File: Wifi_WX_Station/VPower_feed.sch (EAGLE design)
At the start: 5 parts, among them J1 RJ45-8VERT, J2 RJ45-8VERT

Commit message: updated BOM with all prices- As Checked in to BATCH PCB
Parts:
- RAIN, SUN: device wifi_WX:PINHD-1X3 -> wifi_WX:PINHD-1X3MOLEX_KK
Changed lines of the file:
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@@
 <part name="SUPPLY11" library="supply2" deviceset="GND" device=""/>
 <part name="P+3" library="supply1" deviceset="+5V" device=""/>
-<part name="RAIN" library="wifi_WX" deviceset="PINHD-1X3" device=""/>
-<part name="SUN" library="wifi_WX" deviceset="PINHD-1X3" device=""/>
+<part name="RAIN" library="wifi_WX" deviceset="PINHD-1X3" device="MOLEX_KK"/>
+<part name="SUN" library="wifi_WX" deviceset="PINHD-1X3" device="MOLEX_KK"/>
 </parts>
 <sheets>

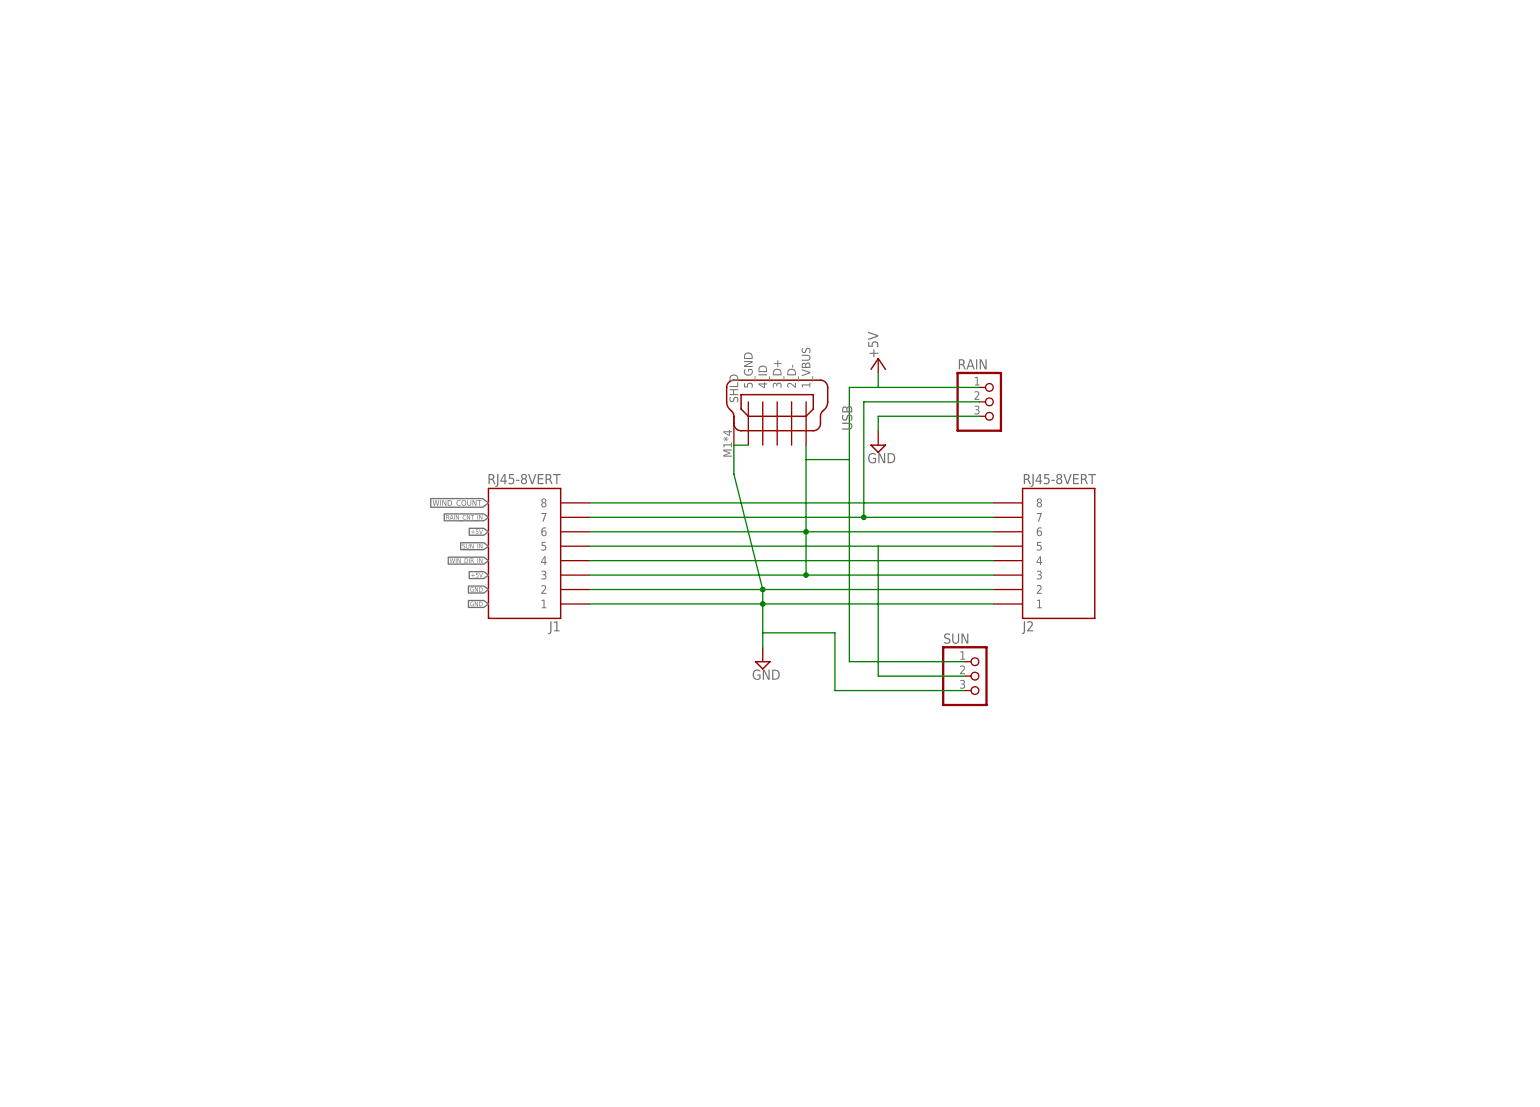
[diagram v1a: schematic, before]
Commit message: added SILabs Hygrometer board Added frames to the schematics
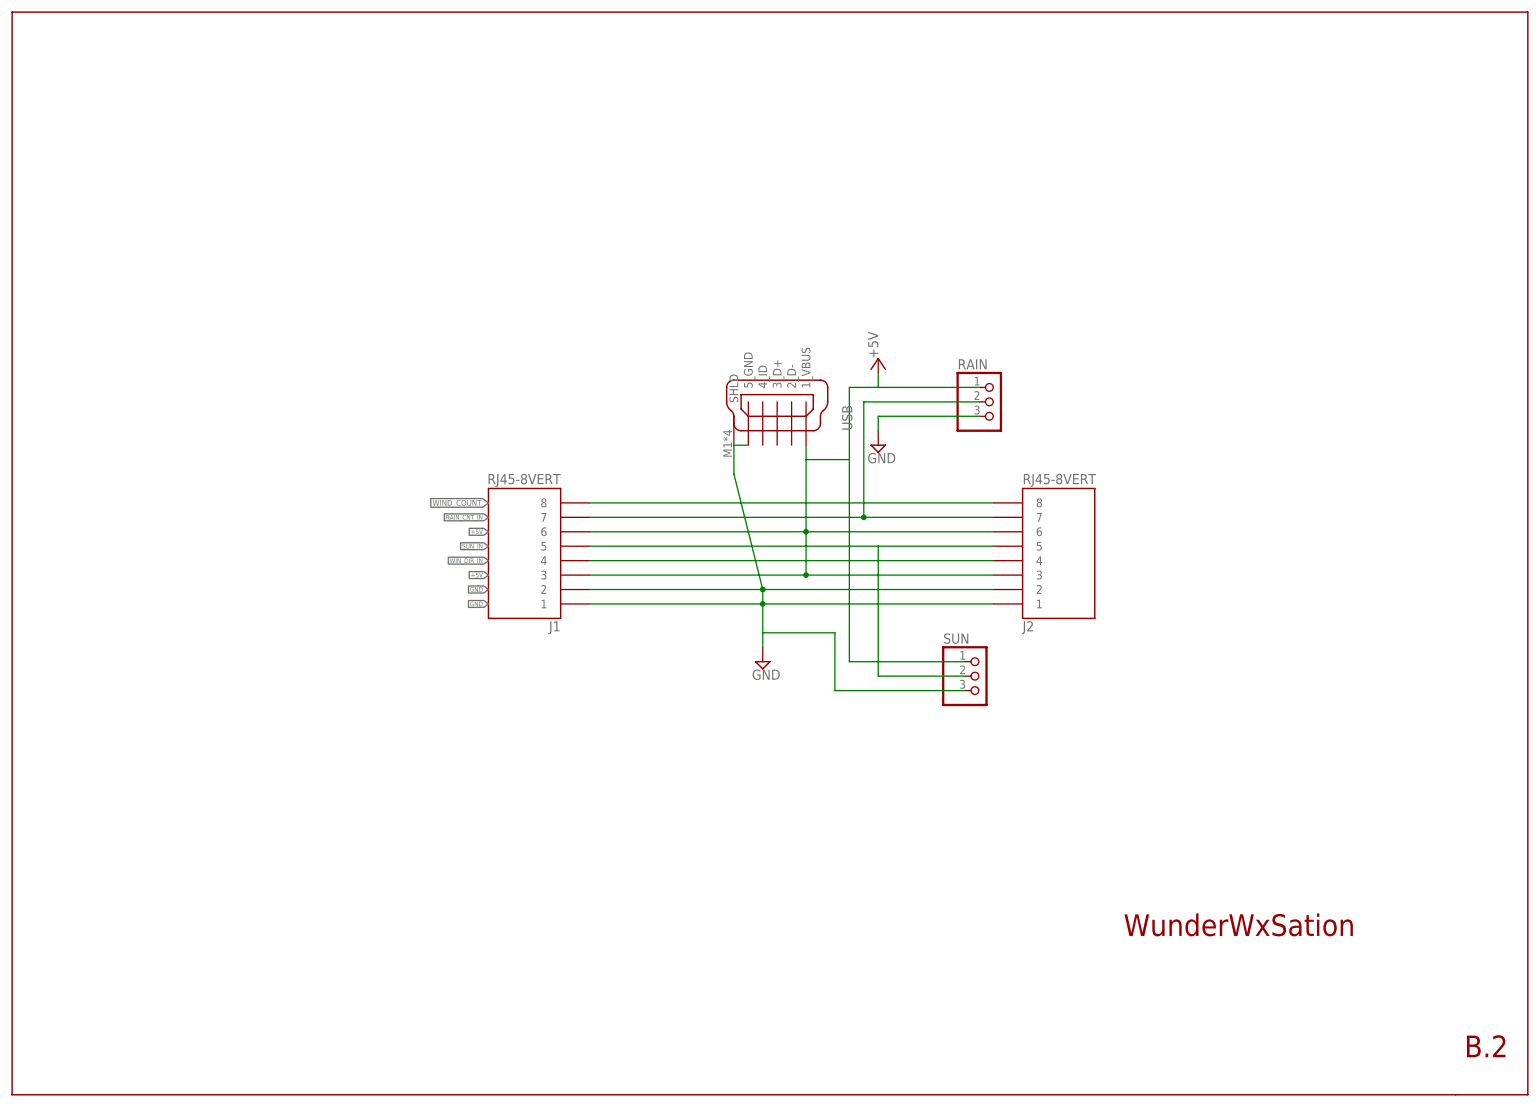
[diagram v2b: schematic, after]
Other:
- note added: "B.2"
- note added: "WunderWxSation"
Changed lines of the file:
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@@
 <part name="RAIN" library="wifi_WX" deviceset="PINHD-1X3" device="MOLEX_KK"/>
 <part name="SUN" library="wifi_WX" deviceset="PINHD-1X3" device="MOLEX_KK"/>
+<part name="U$1" library="1AA_Stofer" deviceset="8.5X11" device=""/>
 </parts>
 <sheets>
 <sheet>
 <plain>
+<text x="119.38" y="-45.72" size="3.81" layer="94" ratio="20">WunderWxSation</text>
+<text x="179.324" y="-67.056" size="3.81" layer="94" ratio="20">B.2</text>
 </plain>
 <instances>
@@
 <instance part="RAIN" gate="A" x="96.52" y="48.26"/>
 <instance part="SUN" gate="A" x="93.98" y="0"/>
+<instance part="U$1" gate="G$1" x="-76.2" y="-73.66"/>
+<instance part="U$1" gate="G$2" x="88.9" y="-73.66"/>
 </instances>
 <busses>
